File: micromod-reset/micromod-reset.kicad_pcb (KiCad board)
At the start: 2 copper layers, 44.5 x 40 mm, 44 parts, among them J1 Conn_01x10, SW1 DFU, SW2 nBOOT, SW3 nRST, SW4 k01, SW5 k02, SW6 k03, SW7 k04, SW8 k05, U1 74LS14, U2 74LS132, U3 74LS08

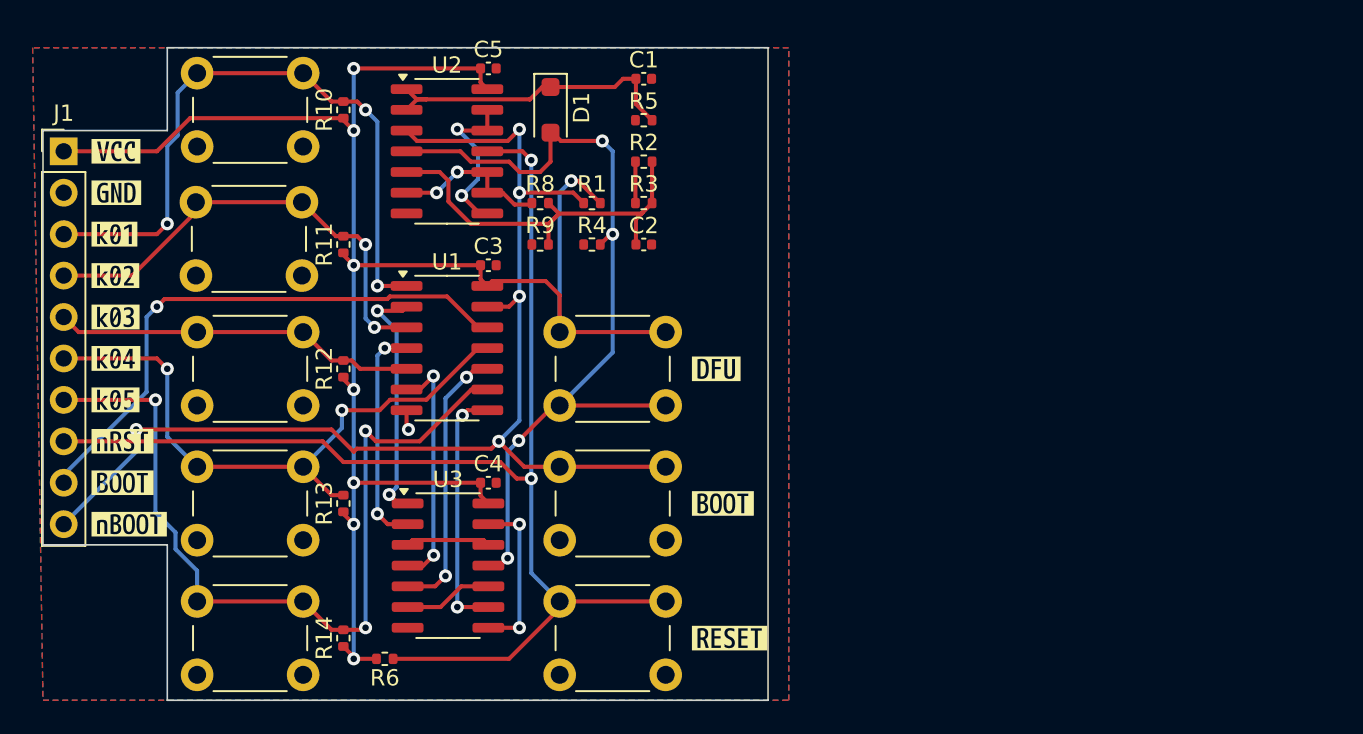
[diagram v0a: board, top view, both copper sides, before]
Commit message: micromod-reset, now with added test points and DRC success
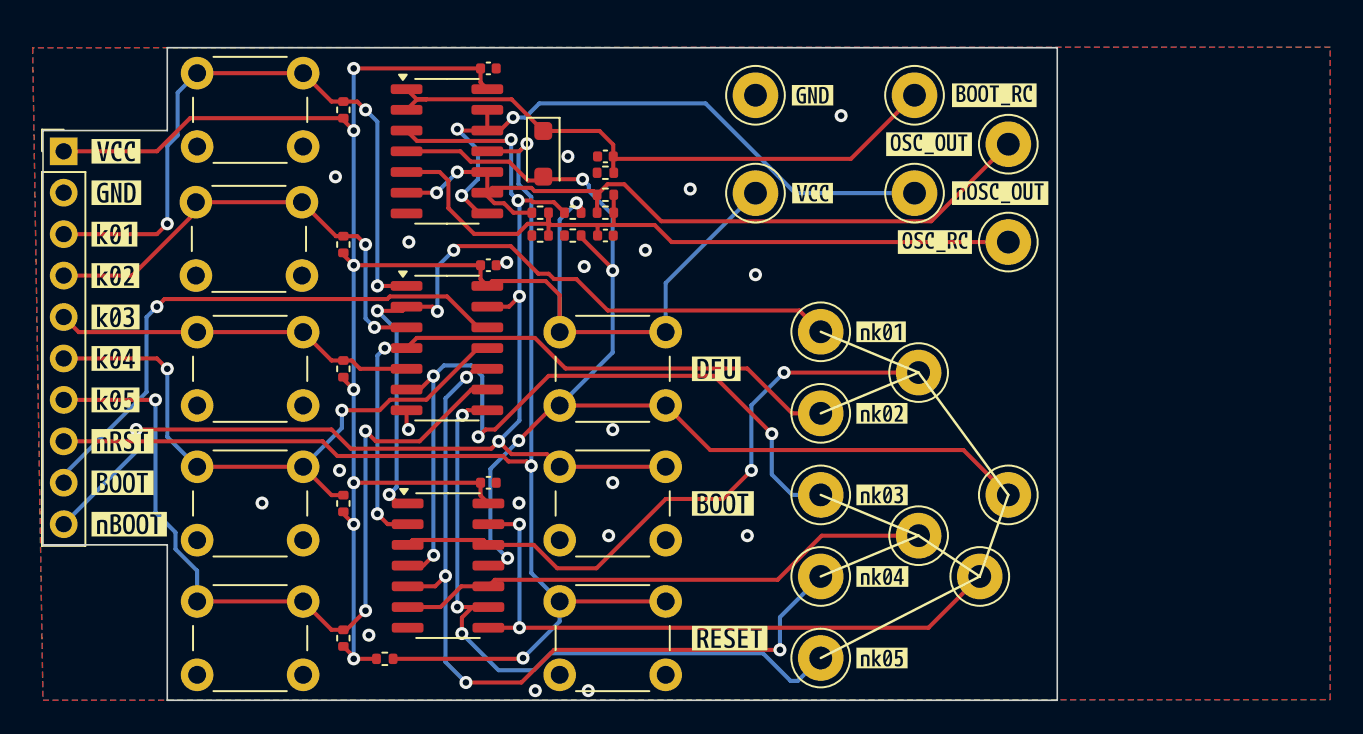
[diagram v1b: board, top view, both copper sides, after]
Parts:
- added TP1: TestPoint_Small, TestPoint:TestPoint_Loop_D3.50mm_Drill1.4mm_Beaded, F.Cu at (153.0, 66.0)
- added TP10: TestPoint_Small, TestPoint:TestPoint_Loop_D3.50mm_Drill1.4mm_Beaded, F.Cu at (158.8, 51.5)
- added TP11: TestPoint_Small, TestPoint:TestPoint_Loop_D3.50mm_Drill1.4mm_Beaded, F.Cu at (164.5, 54.5)
- added TP12: TestPoint_Small, TestPoint:TestPoint_Loop_D3.50mm_Drill1.4mm_Beaded, F.Cu at (164.5, 60.5)
- added TP13: TestPoint_Small, TestPoint:TestPoint_Loop_D3.50mm_Drill1.4mm_Beaded, F.Cu at (158.8, 57.5)
- added TP14: TestPoint_Small, TestPoint:TestPoint_Loop_D3.50mm_Drill1.4mm_Beaded, F.Cu at (149.0, 51.5)
- added TP15: TestPoint_Small, TestPoint:TestPoint_Loop_D3.50mm_Drill1.4mm_Beaded, F.Cu at (149.0, 57.5)
- added TP2: TestPoint_Small, TestPoint:TestPoint_Loop_D3.50mm_Drill1.4mm_Beaded, F.Cu at (153.0, 71.0)
- added TP3: TestPoint_Small, TestPoint:TestPoint_Loop_D3.50mm_Drill1.4mm_Beaded, F.Cu at (153.0, 76.0)
- added TP4: TestPoint_Small, TestPoint:TestPoint_Loop_D3.50mm_Drill1.4mm_Beaded, F.Cu at (153.0, 81.0)
- added TP5: TestPoint_Small, TestPoint:TestPoint_Loop_D3.50mm_Drill1.4mm_Beaded, F.Cu at (153.0, 86.0)
- added TP6: TestPoint_Small, TestPoint:TestPoint_Loop_D3.50mm_Drill1.4mm_Beaded, F.Cu at (159.0, 78.5)
- added TP7: TestPoint_Small, TestPoint:TestPoint_Loop_D3.50mm_Drill1.4mm_Beaded, F.Cu at (159.0, 68.5)
- added TP8: TestPoint_Small, TestPoint:TestPoint_Loop_D3.50mm_Drill1.4mm_Beaded, F.Cu at (162.8, 81.0)
- added TP9: TestPoint_Small, TestPoint:TestPoint_Loop_D3.50mm_Drill1.4mm_Beaded, F.Cu at (164.5, 76.0)
- added kibuzzard-66C2A7CC: G***, kibuzzard-66C2A7CC, F.Cu at (163.6, 51.5)
- added kibuzzard-66C2A80C: G***, kibuzzard-66C2A80C, F.Cu at (160.0, 60.5)
- added kibuzzard-66C2A818: G***, kibuzzard-66C2A818, F.Cu at (164.0, 57.5)
- added kibuzzard-66C2A826: G***, kibuzzard-66C2A826, F.Cu at (159.6, 54.5)
- added kibuzzard-66C2A89E: G***, kibuzzard-66C2A89E, F.Cu at (152.5, 51.5)
- added kibuzzard-66C2A8B2: G***, kibuzzard-66C2A8B2, F.Cu at (152.5, 57.5)
- added kibuzzard-66C2A98F: G***, kibuzzard-66C2A98F, F.Cu at (156.7, 66.0)
- added kibuzzard-66C2A998: G***, kibuzzard-66C2A998, F.Cu at (156.8, 71.0)
- added kibuzzard-66C2A99F: G***, kibuzzard-66C2A99F, F.Cu at (156.8, 76.0)
- added kibuzzard-66C2A9A5: G***, kibuzzard-66C2A9A5, F.Cu at (156.8, 81.0)
- added kibuzzard-66C2A9AD: G***, kibuzzard-66C2A9AD, F.Cu at (156.8, 86.0)
- R1: value 200k -> 10k
- R10: renamed from R11; value 200k -> 10k
- R11: renamed from R12; value 200k -> 10k
- R12: renamed from R13; value 200k -> 10k
- R13: renamed from R14; value 200k -> 10k
- R2: renamed from R4; value 200k -> 10k
- R4: renamed from R6; value 200k -> 10k
- R9: renamed from R10; value 200k -> 10k
- moved C1 5.31 mm to (139.8, 55.2), turned to 180 degrees
- moved R3 3.99 mm to (139.8, 56.2)
- moved R6 3.11 mm to (139.8, 57.6)
- moved D1 2.73 mm to (136.0, 55.1)
- moved R7 2.42 mm to (139.8, 58.7)
- moved C4 2.41 mm to (139.8, 60.1)
- moved R1 1.31 mm to (137.8, 58.7)
- moved R2 1.30 mm to (137.8, 60.1)
- moved R5 0.59 mm to (135.8, 58.7)
- moved R8 0.55 mm to (135.8, 60.1)
- renumbered C3 to C2, C4 to C3, C2 to C4, R5 to R3, R8 to R5, R2 to R6, R3 to R7, R9 to R8
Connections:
- net /~{k07} renamed /~{k02}
- net /~{k17} renamed /~{k04}
- net /~{k23} renamed /~{k05}
- net Net-(C2-Pad1) renamed /OSC_RC
- net Net-(D1-A) renamed /~{k01}&&~{k02}&&~{k03}&&~{k04}&&~{k05}
- net Net-(D1-K) renamed /BOOT_RC
- net Net-(R2-Pad1) renamed /OSC_OUT
- net Net-(U2-Pad12) renamed /~{OSC_OUT}
- net ~{k03}&&~{k07} renamed ~{k01}&&~{k02}
- net ~{k13}&&~{k17} renamed ~{k03}&&~{k04}
- net ~{k13}&&~{k17}&&~{k23} renamed ~{k03}&&~{k04}&&~{k05}
- U1 pad 2: /~{k03} -> /~{k01}
- U1 pad 6: /~{k13} -> /~{k03}
- U3 pad 1: /~{k03} -> /~{k01}
- U3 pad 4: /~{k13} -> /~{k03}
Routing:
- net /~{k01}: track 0.00 -> 46.1 mm, vias 0 -> 4
- net ~{k01}&&~{k02}: track 5.20 -> 39.5 mm, vias 0 -> 2
- net /OSC_OUT: track 12.4 -> 46.6 mm
- net /~{k03}: track 15.2 -> 49.2 mm, vias 2 -> 4
- net /~{k04}: track 16.8 -> 49.5 mm, vias 2 -> 4
- net ~{k03}&&~{k04}&&~{k05}: track 11.4 -> 41.0 mm
- net /~{OSC_OUT}: track 10.2 -> 39.3 mm, vias 2 -> 3
- net ~{k03}&&~{k04}: track 5.48 -> 33.1 mm
- net /~{k02}: track 13.8 -> 41.4 mm
- net /~{k05}: track 15.4 -> 43.0 mm, vias 2 -> 3
- net /~{k01}&&~{k02}&&~{k03}&&~{k04}&&~{k05}: track 52.4 -> 73.5 mm
- net /OSC_RC: track 25.4 -> 45.0 mm
- net /BOOT_RC: track 19.3 -> 37.4 mm
- net /~{k13}: track 14.8 -> 0.00 mm, vias 2 -> 0
- net +3V3: track 114.0 -> 121.9 mm
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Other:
- board size 44.5 x 40 mm -> 62.2 x 40 mm

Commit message: Updated JLC to match fixed circuit.
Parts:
- R1, R10, R11, R12, R13, R2, R4, R9: value 10k -> 200k
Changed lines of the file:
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@@
 				(font
 					(size 0.001 0.001)
+					(thickness 0.15)
 				)
 			)
@@
 				(font
 					(size 0.001 0.001)
+					(thickness 0.15)
 				)
 			)
@@
 			)
 		)
-		(property "Value" "10k"
+		(property "Value" "200k"
 			(at 0 1.17 90)
 			(layer "F.Fab")
@@
 			)
 		)
-		(property "Value" "10k"
+		(property "Value" "200k"
 			(at 0 1.17 90)
 			(layer "F.Fab")
@@
 			)
 		)
-		(property "Value" "10k"
+		(property "Value" "200k"
 			(at 0 1.17 0)
 			(layer "F.Fab")
@@
 			)
 		)
-		(property "Value" "10k"
+		(property "Value" "200k"
 			(at 0 1.17 90)
 			(layer "F.Fab")
@@
 				(font
 					(size 0.001 0.001)
+					(thickness 0.15)
 				)
 			)
@@
 				(font
 					(size 0.001 0.001)
+					(thickness 0.15)
 				)
 			)
@@
 				(font
 					(size 0.001 0.001)
+					(thickness 0.15)
 				)
 			)
@@
 				(font
 					(size 0.001 0.001)
+					(thickness 0.15)
 				)
 			)
@@
 			)
 		)
-		(property "Value" "10k"
+		(property "Value" "200k"
 			(at 0 1.17 0)
 			(layer "F.Fab")
@@
 				(font
 					(size 0.001 0.001)
+					(thickness 0.15)
 				)
 			)
@@
 				(font
 					(size 0.001 0.001)
+					(thickness 0.15)
 				)
 			)
@@
 			)
 		)
-		(property "Value" "10k"
+		(property "Value" "200k"
 			(at 0 1.17 90)
 			(layer "F.Fab")
@@
 				(font
 					(size 0.001 0.001)
+					(thickness 0.15)
 				)
 			)
@@
 				(font
 					(size 0.001 0.001)
+					(thickness 0.15)
 				)
 			)
@@
 			)
 		)
-		(property "Value" "10k"
+		(property "Value" "200k"
 			(at 0 1.17 90)
 			(layer "F.Fab")
@@
 				(font
 					(size 0.001 0.001)
+					(thickness 0.15)
 				)
 			)
@@
 				(font
 					(size 0.001 0.001)
+					(thickness 0.15)
 				)
 			)
@@
 				(font
 					(size 0.001 0.001)
+					(thickness 0.15)
 				)
 			)
@@
 				(font
 					(size 0.001 0.001)
+					(thickness 0.15)
 				)
 			)
@@
 				(font
 					(size 0.001 0.001)
+					(thickness 0.15)
 				)
 			)
@@
 				(font
 					(size 0.001 0.001)
+					(thickness 0.15)
 				)
 			)
@@
 			)
 		)
-		(property "Value" "10k"
+		(property "Value" "200k"
 			(at 0 1.17 0)
 			(layer "F.Fab")
@@
 				(font
 					(size 0.001 0.001)
+					(thickness 0.15)
 				)
 			)
@@
 				(font
 					(size 0.001 0.001)
+					(thickness 0.15)
 				)
 			)
@@
 				(font
 					(size 0.001 0.001)
+					(thickness 0.15)
 				)
 			)
@@
 				(font
 					(size 0.001 0.001)
+					(thickness 0.15)
 				)
 			)
@@
 				(font
 					(size 0.001 0.001)
+					(thickness 0.15)
 				)
 			)
@@
 				(font
 					(size 0.001 0.001)
+					(thickness 0.15)
 				)
 			)
